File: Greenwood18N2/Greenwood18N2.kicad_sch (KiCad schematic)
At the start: 244 parts, among them SW1 RotaryEncoder_Switch, SW10 Switch w/LED, SW100 Switch w/LED, SW101 Switch w/LED, SW102 Switch w/LED, SW103 Switch w/LED, SW104 Switch w/LED, SW105 Switch w/LED, SW106 Switch w/LED, SW107 Switch w/LED, SW108 Switch w/LED, SW109 Switch w/LED, SW11 Switch w/LED, SW110 Switch w/LED, SW12 Switch w/LED, SW13 Switch w/LED, SW14 Switch w/LED, SW15 Switch w/LED, SW16 Switch w/LED, SW17 Switch w/LED, SW18 Switch w/LED, SW19 RotaryEncoder_Switch, SW2 Switch w/LED, SW20 Switch w/LED, SW21 Switch w/LED, SW22 Switch w/LED, SW23 Switch w/LED, SW24 Switch w/LED, SW25 Switch w/LED, SW26 Switch w/LED, SW27 Switch w/LED, SW28 Switch w/LED, SW29 Switch w/LED, SW3 Switch w/LED, SW30 Switch w/LED, SW31 Switch w/LED, SW32 Switch w/LED, SW33 Switch w/LED, SW34 Switch w/LED, SW35 Switch w/LED, SW36 Switch w/LED, SW37 Switch w/LED, SW38 Switch w/LED, SW39 Switch w/LED, SW4 Switch w/LED, SW40 Switch w/LED, SW41 Switch w/LED, SW42 Switch w/LED, SW43 Switch w/LED, SW44 Switch w/LED, SW45 Switch w/LED, SW46 Switch w/LED, SW47 Switch w/LED, SW48 Switch w/LED, SW49 Switch w/LED, SW5 Switch w/LED, SW50 Switch w/LED, SW51 Switch w/LED, SW52 Switch w/LED, SW53 Switch w/LED, SW54 Switch w/LED, SW55 Switch w/LED, SW56 Switch w/LED, SW57 Switch w/LED, SW58 Switch w/LED, SW59 Switch w/LED, SW6 Switch w/LED, SW60 Switch w/LED, SW61 RotaryEncoder_Switch, SW62 Switch w/LED, SW63 Switch w/LED, SW64 Switch w/LED, SW65 Switch w/LED, SW66 Switch w/LED, SW67 Switch w/LED, SW68 Switch w/LED, SW69 Switch w/LED, SW7 Switch w/LED, SW70 Switch w/LED, SW71 Switch w/LED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

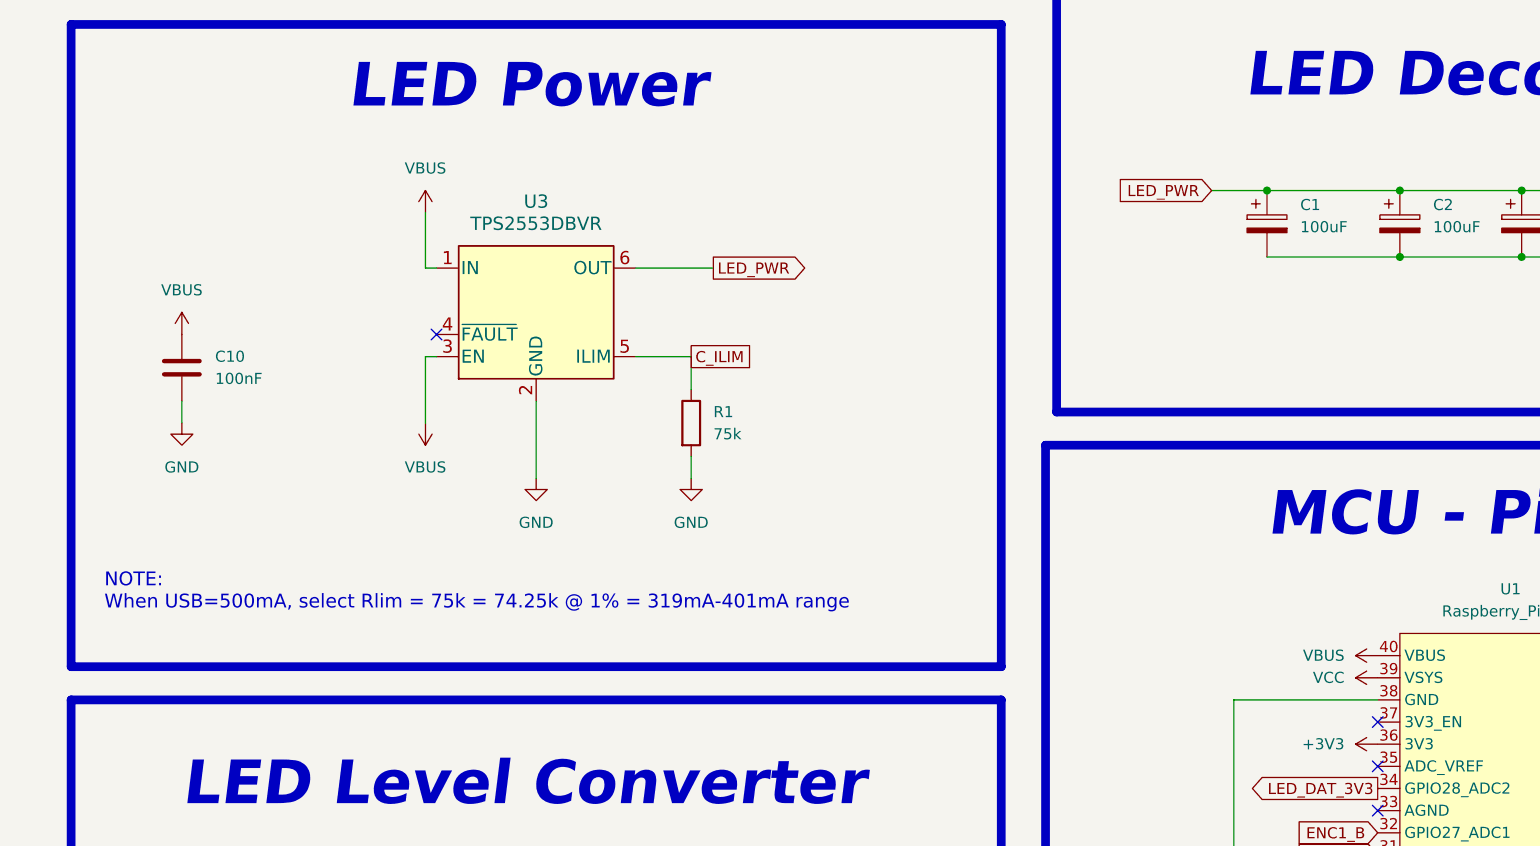
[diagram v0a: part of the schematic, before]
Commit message: Add .pretty for KiCAD
- _mod files added
- 3D models added
- update keyboard name in schematics to match
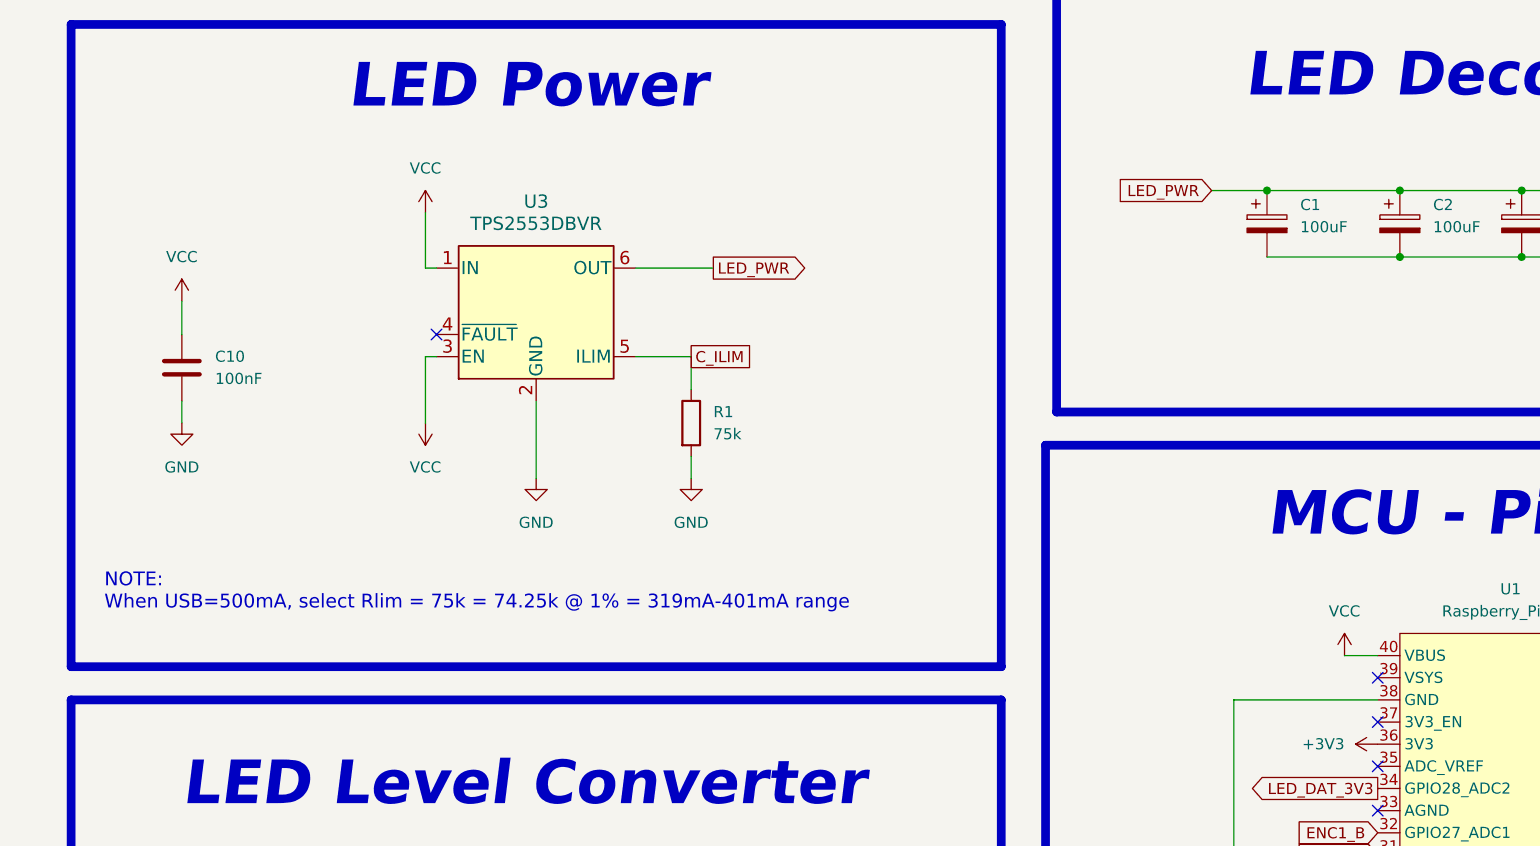
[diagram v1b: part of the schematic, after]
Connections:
- net VBUS is gone; now on net VCC: C10.2, U1.40 (VBUS), U3.1 (IN), U3.3 (EN)
- net VCC: no longer U1.39 (VSYS)
- no-connect marks 8 -> 9
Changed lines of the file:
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@@
   (no_connect (at 270.51 138.43))
   (no_connect (at 270.51 120.65))
+  (no_connect (at 270.51 115.57))
   (no_connect (at 162.56 76.2))
   (no_connect (at 270.51 130.81))
@@
     (stroke (width 0) (type default))
   )
+  (wire (pts (xy 133.35 72.39) (xy 133.35 76.2))
+    (stroke (width 0) (type default))
+  )
   (wire (pts (xy 300.99 156.21) (xy 318.77 156.21))
     (stroke (width 0) (type default))
@@
     (stroke (width 0) (type default))
   )
+  (wire (pts (xy 266.7 113.03) (xy 270.51 113.03))
+    (stroke (width 0) (type default))
+  )
   (wire (pts (xy 144.78 326.39) (xy 144.78 356.87))
     (stroke (width 0) (type default))
@@
     )
   )
+  (symbol (lib_id "power:VCC") (at 161.29 86.36 180) (unit 1)
+    (in_bom yes) (on_board yes) (dnp no) (fields_autoplaced)
+    (property "Reference" "#PWR016" (at 161.29 82.55 0)
+      (effects (font (size 1.27 1.27)) hide)
+    )
+    (property "Value" "VCC" (at 161.29 91.44 0)
+      (effects (font (size 1.27 1.27)))
+    )
+    (property "Footprint" "" (at 161.29 86.36 0)
+      (effects (font (size 1.27 1.27)) hide)
+    )
+    (property "Datasheet" "" (at 161.29 86.36 0)
+      (effects (font (size 1.27 1.27)) hide)
+    )
+    (pin "1")
+    (instances
+      (project "Greenwood18N2"
+        (path "/9efe463e-e9e8-4c7d-9e2c-b657456ce19f"
+          (reference "#PWR016") (unit 1)
+        )
+      )
+    )
+  )
   (symbol (lib_id "ScottoKeebs:Placeholder_Diode") (at 525.78 247.65 90) (unit 1)
     (in_bom yes) (on_board yes) (dnp no) (fields_autoplaced)
@@
     )
   )
-  (symbol (lib_id "power:VBUS") (at 133.35 76.2 0) (unit 1)
-    (in_bom yes) (on_board yes) (dnp no) (fields_autoplaced)
-    (property "Reference" "#PWR022" (at 133.35 80.01 0)
-      (effects (font (size 1.27 1.27)) hide)
-    )
-    (property "Value" "VBUS" (at 133.35 71.12 0)
-      (effects (font (size 1.27 1.27)))
-    )
-    (property "Footprint" "" (at 133.35 76.2 0)
-      (effects (font (size 1.27 1.27)) hide)
-    )
-    (property "Datasheet" "" (at 133.35 76.2 0)
-      (effects (font (size 1.27 1.27)) hide)
-    )
-    (pin "1")
-    (instances
-      (project "Greenwood18N2"
-        (path "/9efe463e-e9e8-4c7d-9e2c-b657456ce19f"
-          (reference "#PWR022") (unit 1)
-        )
-      )
-    )
-  )
   (symbol (lib_id "ScottoKeebs:Placeholder_Diode") (at 449.58 381 270) (unit 1)
     (in_bom yes) (on_board yes) (dnp no) (fields_autoplaced)
@@
     )
   )
+  (symbol (lib_id "power:VCC") (at 161.29 62.23 0) (unit 1)
+    (in_bom yes) (on_board yes) (dnp no) (fields_autoplaced)
+    (property "Reference" "#PWR019" (at 161.29 66.04 0)
+      (effects (font (size 1.27 1.27)) hide)
+    )
+    (property "Value" "VCC" (at 161.29 57.15 0)
+      (effects (font (size 1.27 1.27)))
+    )
+    (property "Footprint" "" (at 161.29 62.23 0)
+      (effects (font (size 1.27 1.27)) hide)
+    )
+    (property "Datasheet" "" (at 161.29 62.23 0)
+      (effects (font (size 1.27 1.27)) hide)
+    )
+    (pin "1")
+    (instances
+      (project "Greenwood18N2"
+        (path "/9efe463e-e9e8-4c7d-9e2c-b657456ce19f"
+          (reference "#PWR019") (unit 1)
+        )
+      )
+    )
+  )
   (symbol (lib_id "ScottoKeebs:Placeholder_Diode") (at 195.58 425.45 90) (unit 1)
     (in_bom yes) (on_board yes) (dnp no) (fields_autoplaced)
@@
     )
   )
-  (symbol (lib_id "power:VBUS") (at 161.29 86.36 180) (unit 1)
-    (in_bom yes) (on_board yes) (dnp no) (fields_autoplaced)
-    (property "Reference" "#PWR016" (at 161.29 82.55 0)
-      (effects (font (size 1.27 1.27)) hide)
-    )
-    (property "Value" "VBUS" (at 161.29 91.44 0)
-      (effects (font (size 1.27 1.27)))
-    )
-    (property "Footprint" "" (at 161.29 86.36 0)
-      (effects (font (size 1.27 1.27)) hide)
-    )
-    (property "Datasheet" "" (at 161.29 86.36 0)
-      (effects (font (size 1.27 1.27)) hide)
-    )
-    (pin "1")
-    (instances
-      (project "Greenwood18N2"
-        (path "/9efe463e-e9e8-4c7d-9e2c-b657456ce19f"
-          (reference "#PWR016") (unit 1)
-        )
-      )
-    )
-  )
   (symbol (lib_id "ScottoKeebs:Placeholder_Diode") (at 551.18 292.1 270) (unit 1)
     (in_bom yes) (on_board yes) (dnp no) (fields_autoplaced)
@@
     )
   )
+  (symbol (lib_id "power:VCC") (at 133.35 72.39 0) (unit 1)
+    (in_bom yes) (on_board yes) (dnp no) (fields_autoplaced)
+    (property "Reference" "#PWR021" (at 133.35 76.2 0)
+      (effects (font (size 1.27 1.27)) hide)
+    )
+    (property "Value" "VCC" (at 133.35 67.31 0)
+      (effects (font (size 1.27 1.27)))
+    )
+    (property "Footprint" "" (at 133.35 72.39 0)
+      (effects (font (size 1.27 1.27)) hide)
+    )
+    (property "Datasheet" "" (at 133.35 72.39 0)
+      (effects (font (size 1.27 1.27)) hide)
+    )
+    (pin "1")
+    (instances
+      (project "Greenwood18N2"
+        (path "/9efe463e-e9e8-4c7d-9e2c-b657456ce19f"
+          (reference "#PWR021") (unit 1)
+        )
+      )
+    )
+  )
   (symbol (lib_id "ScottoKeebs:Placeholder_Diode") (at 627.38 292.1 90) (unit 1)
     (in_bom yes) (on_board yes) (dnp no) (fields_autoplaced)
@@
     )
   )
-  (symbol (lib_id "power:VCC") (at 270.51 115.57 90) (unit 1)
-    (in_bom yes) (on_board yes) (dnp no) (fields_autoplaced)
-    (property "Reference" "#PWR019" (at 274.32 115.57 0)
-      (effects (font (size 1.27 1.27)) hide)
-    )
-    (property "Value" "VCC" (at 266.7 115.57 90)
-      (effects (font (size 1.27 1.27)) (justify left))
-    )
-    (property "Footprint" "" (at 270.51 115.57 0)
-      (effects (font (size 1.27 1.27)) hide)
-    )
-    (property "Datasheet" "" (at 270.51 115.57 0)
-      (effects (font (size 1.27 1.27)) hide)
-    )
-    (pin "1")
-    (instances
-      (project "Greenwood18N2"
-        (path "/9efe463e-e9e8-4c7d-9e2c-b657456ce19f"
-          (reference "#PWR019") (unit 1)
-        )
-      )
-    )
-  )
   (symbol (lib_id "KeebLib:Switch w/LED") (at 601.98 473.71 0) (unit 1)
     (in_bom yes) (on_board yes) (dnp no)
@@
     )
   )
-  (symbol (lib_id "power:VBUS") (at 270.51 113.03 90) (unit 1)
-    (in_bom yes) (on_board yes) (dnp no) (fields_autoplaced)
-    (property "Reference" "#PWR015" (at 274.32 113.03 0)
-      (effects (font (size 1.27 1.27)) hide)
-    )
-    (property "Value" "VBUS" (at 266.7 113.03 90)
-      (effects (font (size 1.27 1.27)) (justify left))
-    )
-    (property "Footprint" "" (at 270.51 113.03 0)
-      (effects (font (size 1.27 1.27)) hide)
-    )
-    (property "Datasheet" "" (at 270.51 113.03 0)
-      (effects (font (size 1.27 1.27)) hide)
-    )
-    (pin "1")
-    (instances
-      (project "Greenwood18N2"
-        (path "/9efe463e-e9e8-4c7d-9e2c-b657456ce19f"
-          (reference "#PWR015") (unit 1)
-        )
-      )
-    )
-  )
   (symbol (lib_id "KeebLib:Switch w/LED") (at 347.98 295.91 0) (unit 1)
     (in_bom yes) (on_board yes) (dnp no)
@@
     )
   )
+  (symbol (lib_id "power:VCC") (at 266.7 113.03 0) (unit 1)
+    (in_bom yes) (on_board yes) (dnp no) (fields_autoplaced)
+    (property "Reference" "#PWR015" (at 266.7 116.84 0)
+      (effects (font (size 1.27 1.27)) hide)
+    )
+    (property "Value" "VCC" (at 266.7 107.95 0)
+      (effects (font (size 1.27 1.27)))
+    )
+    (property "Footprint" "" (at 266.7 113.03 0)
+      (effects (font (size 1.27 1.27)) hide)
+    )
+    (property "Datasheet" "" (at 266.7 113.03 0)
+      (effects (font (size 1.27 1.27)) hide)
+    )
+    (pin "1")
+    (instances
+      (project "Greenwood18N2"
+        (path "/9efe463e-e9e8-4c7d-9e2c-b657456ce19f"
+          (reference "#PWR015") (unit 1)
+        )
+      )
+    )
+  )
   (symbol (lib_id "power:GND") (at 133.35 86.36 0) (unit 1)
     (in_bom yes) (on_board yes) (dnp no) (fields_autoplaced)
@@
         )
       )
-    )
-  )
-  (symbol (lib_id "power:VBUS") (at 161.29 62.23 0) (unit 1)
-    (in_bom yes) (on_board yes) (dnp no) (fields_autoplaced)
-    (property "Reference" "#PWR021" (at 161.29 66.04 0)
-      (effects (font (size 1.27 1.27)) hide)
-    )
-    (property "Value" "VBUS" (at 161.29 57.15 0)
-      (effects (font (size 1.27 1.27)))
-    )
-    (property "Footprint" "" (at 161.29 62.23 0)
-      (effects (font (size 1.27 1.27)) hide)
-    )
-    (property "Datasheet" "" (at 161.29 62.23 0)
-      (effects (font (size 1.27 1.27)) hide)
-    )
-    (pin "1")
-    (instances
-      (project "Greenwood18N2"
-        (path "/9efe463e-e9e8-4c7d-9e2c-b657456ce19f"
-          (reference "#PWR021") (unit 1)
-        )
-      )

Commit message: Current Limiter update
add in an RC delay circuit for the EN pin of the TPS2553 current limiter. This should allow the USB to handshake and configure itself and the allow the current limiter to then start working.
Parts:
- added C2: 100nF, Capacitor_SMD:C_1206_3216Metric_Pad1.33x1.80mm_HandSolder, symbol Device:C
- added R1: 220k - 5.1M, Resistor_SMD:R_1206_3216Metric_Pad1.30x1.75mm_HandSolder, symbol Device:R
- OLED1: footprint KeebLib:OLED_ST7735_2inch -> Greenwood:OLED_ST7735_2inch
- SW1: renamed from SW2; footprint KeebLib:Hotswap_MX_Plated_LED_1u -> Greenwood:Hotswap_MX_Plated_LED_1u
- SW10: renamed from SW11; footprint KeebLib:Hotswap_MX_Plated_LED_1u -> Greenwood:Hotswap_MX_Plated_LED_1u
- SW100: footprint KeebLib:Hotswap_MX_Plated_LED_1.25u -> Greenwood:Hotswap_MX_Plated_LED_1.25u
- SW101, SW80: footprint KeebLib:Hotswap_MX_Plated_LED_2.25u -> Greenwood:Hotswap_MX_Plated_LED_2.25u
- SW102, SW103, SW104, SW105, SW106, SW107, SW108, SW109, SW110, SW20, SW21, SW22, SW23, SW24, SW25, SW26, SW27, SW28, SW29, SW30, SW31, SW32, SW33, SW34, SW35, SW36, SW38, SW40, SW41, SW42, SW44, SW45, SW46, SW47, SW48, SW49, SW50, SW51, SW52, SW53, SW54, SW55, SW57, SW58, SW59, SW60, SW77, SW78, SW79, SW81, SW82, SW83, SW84, SW85, SW86, SW87, SW88, SW89, SW90, SW92, SW93, SW94, SW95, SW96: footprint KeebLib:Hotswap_MX_Plated_LED_1u -> Greenwood:Hotswap_MX_Plated_LED_1u
- SW11: renamed from SW12; footprint KeebLib:Hotswap_MX_Plated_LED_1u -> Greenwood:Hotswap_MX_Plated_LED_1u
- SW12: renamed from SW13; footprint KeebLib:Hotswap_MX_Plated_LED_1u -> Greenwood:Hotswap_MX_Plated_LED_1u
- SW13: renamed from SW14; footprint KeebLib:Hotswap_MX_Plated_LED_1u -> Greenwood:Hotswap_MX_Plated_LED_1u
- SW14: renamed from SW15; footprint KeebLib:Hotswap_MX_Plated_LED_1u -> Greenwood:Hotswap_MX_Plated_LED_1u
- SW15: renamed from SW16; footprint KeebLib:Hotswap_MX_Plated_LED_1u -> Greenwood:Hotswap_MX_Plated_LED_1u
- SW16: renamed from SW17; footprint KeebLib:Hotswap_MX_Plated_LED_1u -> Greenwood:Hotswap_MX_Plated_LED_1u
- SW17: renamed from SW18; footprint KeebLib:Hotswap_MX_Plated_LED_1u -> Greenwood:Hotswap_MX_Plated_LED_1u
- SW18: renamed from SW1; footprint KeebLib:ROT_Alps_EC11E-Hotswap_LED -> Greenwood:ROT_Alps_EC11E-Hotswap_LED
- SW19: footprint KeebLib:ROT_Alps_EC11E-Hotswap_LED -> Greenwood:ROT_Alps_EC11E-Hotswap_LED
- SW2: renamed from SW3; footprint KeebLib:Hotswap_MX_Plated_LED_1u -> Greenwood:Hotswap_MX_Plated_LED_1u
- SW3: renamed from SW4; footprint KeebLib:Hotswap_MX_Plated_LED_1u -> Greenwood:Hotswap_MX_Plated_LED_1u
- SW37: footprint KeebLib:Hotswap_MX_Plated_LED_2u -> Greenwood:Hotswap_MX_Plated_LED_1u
- SW39, SW76: footprint KeebLib:Hotswap_MX_Plated_LED_2u_90deg -> Greenwood:Hotswap_MX_Plated_LED_2u_90deg
- SW4: renamed from SW5; footprint KeebLib:Hotswap_MX_Plated_LED_1u -> Greenwood:Hotswap_MX_Plated_LED_1u
- SW43, SW56, SW97, SW98: footprint KeebLib:Hotswap_MX_Plated_LED_1.5u -> Greenwood:Hotswap_MX_Plated_LED_1.5u
- SW5: renamed from SW6; footprint KeebLib:Hotswap_MX_Plated_LED_1u -> Greenwood:Hotswap_MX_Plated_LED_1u
- SW6: renamed from SW7; footprint KeebLib:Hotswap_MX_Plated_LED_1u -> Greenwood:Hotswap_MX_Plated_LED_1u
- SW61: renamed from SW62; footprint KeebLib:Hotswap_MX_Plated_LED_1.75u -> Greenwood:Hotswap_MX_Plated_LED_1.75u
- SW62: renamed from SW63; footprint KeebLib:Hotswap_MX_Plated_LED_1u -> Greenwood:Hotswap_MX_Plated_LED_1u
- SW63: renamed from SW64; footprint KeebLib:Hotswap_MX_Plated_LED_1u -> Greenwood:Hotswap_MX_Plated_LED_1u
- SW64: renamed from SW65; footprint KeebLib:Hotswap_MX_Plated_LED_1u -> Greenwood:Hotswap_MX_Plated_LED_1u
- SW65: renamed from SW66; footprint KeebLib:Hotswap_MX_Plated_LED_1u -> Greenwood:Hotswap_MX_Plated_LED_1u
- SW66: renamed from SW67; footprint KeebLib:Hotswap_MX_Plated_LED_1u -> Greenwood:Hotswap_MX_Plated_LED_1u
- SW67: renamed from SW68; footprint KeebLib:Hotswap_MX_Plated_LED_1u -> Greenwood:Hotswap_MX_Plated_LED_1u
- SW68: renamed from SW69; footprint KeebLib:Hotswap_MX_Plated_LED_1u -> Greenwood:Hotswap_MX_Plated_LED_1u
- SW69: renamed from SW70; footprint KeebLib:Hotswap_MX_Plated_LED_1u -> Greenwood:Hotswap_MX_Plated_LED_1u
- SW7: renamed from SW8; footprint KeebLib:Hotswap_MX_Plated_LED_1u -> Greenwood:Hotswap_MX_Plated_LED_1u
- SW70: renamed from SW71; footprint KeebLib:Hotswap_MX_Plated_LED_1u -> Greenwood:Hotswap_MX_Plated_LED_1u
- SW71: renamed from SW72; footprint KeebLib:Hotswap_MX_Plated_LED_1u -> Greenwood:Hotswap_MX_Plated_LED_1u
- SW72: renamed from SW73; footprint KeebLib:Hotswap_MX_Plated_LED_1u -> Greenwood:Hotswap_MX_Plated_LED_1u
- SW73: renamed from SW74; footprint KeebLib:Hotswap_MX_Plated_LED_2.25u -> Greenwood:Hotswap_MX_Plated_LED_2.25u
- SW74: renamed from SW75; footprint KeebLib:Hotswap_MX_Plated_LED_1u -> Greenwood:Hotswap_MX_Plated_LED_1u
- SW75: renamed from SW61; footprint KeebLib:ROT_Alps_EC11E-Hotswap_LED -> Greenwood:ROT_Alps_EC11E-Hotswap_LED
- SW8: renamed from SW9; footprint KeebLib:Hotswap_MX_Plated_LED_1u -> Greenwood:Hotswap_MX_Plated_LED_1u
- SW9: renamed from SW10; footprint KeebLib:Hotswap_MX_Plated_LED_1u -> Greenwood:Hotswap_MX_Plated_LED_1u
- SW91: footprint KeebLib:Hotswap_MX_Plated_LED_1.75u -> Greenwood:Hotswap_MX_Plated_LED_1.75u
- SW99: footprint KeebLib:Hotswap_MX_Plated_LED_2.75u -> Greenwood:Hotswap_MX_Plated_LED_2.75u
- U2: renamed from U1; footprint KeebLib:Raspberry_Pi_Pico_Flipped -> Greenwood:Raspberry_Pi_Pico_Flipped
- renumbered C10 to C1, C3 to C10, C4 to C11, C5 to C12, C11 to C3, C6 to C4, C7 to C5, C8 to C6, C9 to C7, C1 to C8, C2 to C9, R1 to R2, U3 to U1, U2 to U3
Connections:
- net GND: now also C2.1
- net VCC: now also R1.1; no longer U1.3 (EN)
- new net: C2.2, R1.2, U1.3 (EN)
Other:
- note added: "NOTE: When USB=500mA, select Rlim = 75k = 74.25k @ 1% = 319mA-401mA range RC circuit to delay EN pin signal when pluggin in USB, t = RC t is for ~62% of input Voltage. 220k gives ~0.2s. 5.1M gives ~0.5s"
- note removed: "NOTE: When USB=500mA, select Rlim = 75k = 74.25k @ 1% = 319mA-401mA range"
- moved on the sheet: C1
